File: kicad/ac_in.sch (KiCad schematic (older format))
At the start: 32 parts, among them J701 tblock, U702 R-78E3.3-1.0, U704 R-78E5.0-1.0, U705 AP2114H-1.2TRG1, U706 AP2114H-1.2TRG1

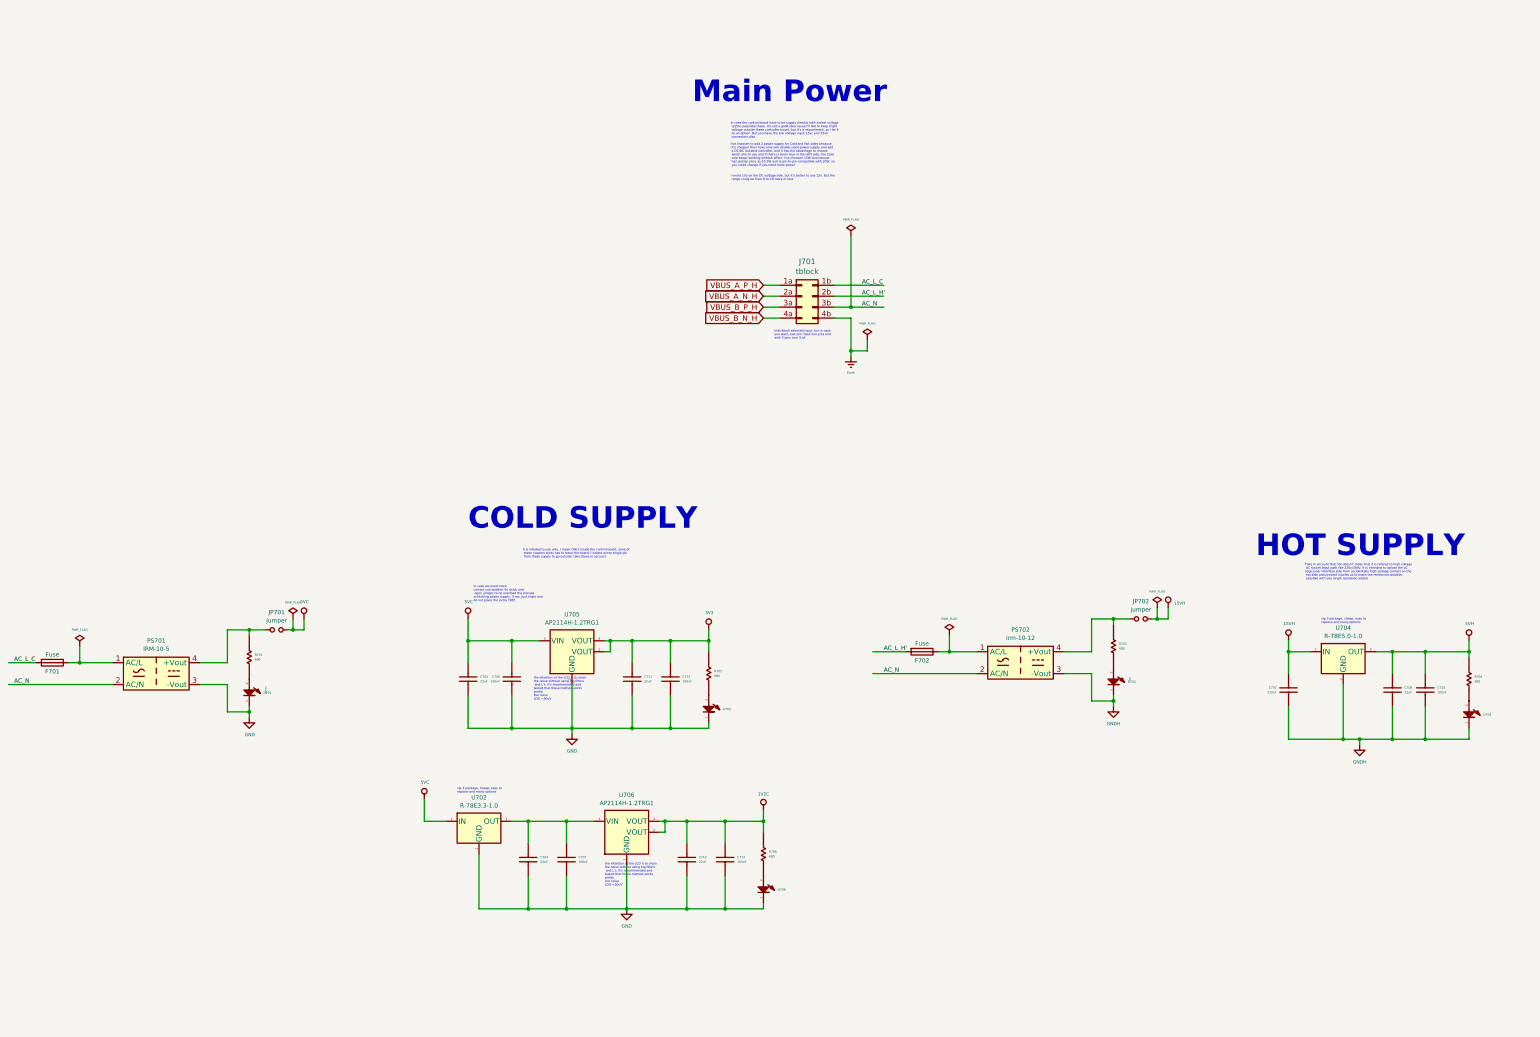
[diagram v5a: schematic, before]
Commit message: mofifing ac/dc position and 3 idc out to 2
I've triung to reacomodate the ac/dc power supplies to manage isolation
and free space using 2 idc instead of 3
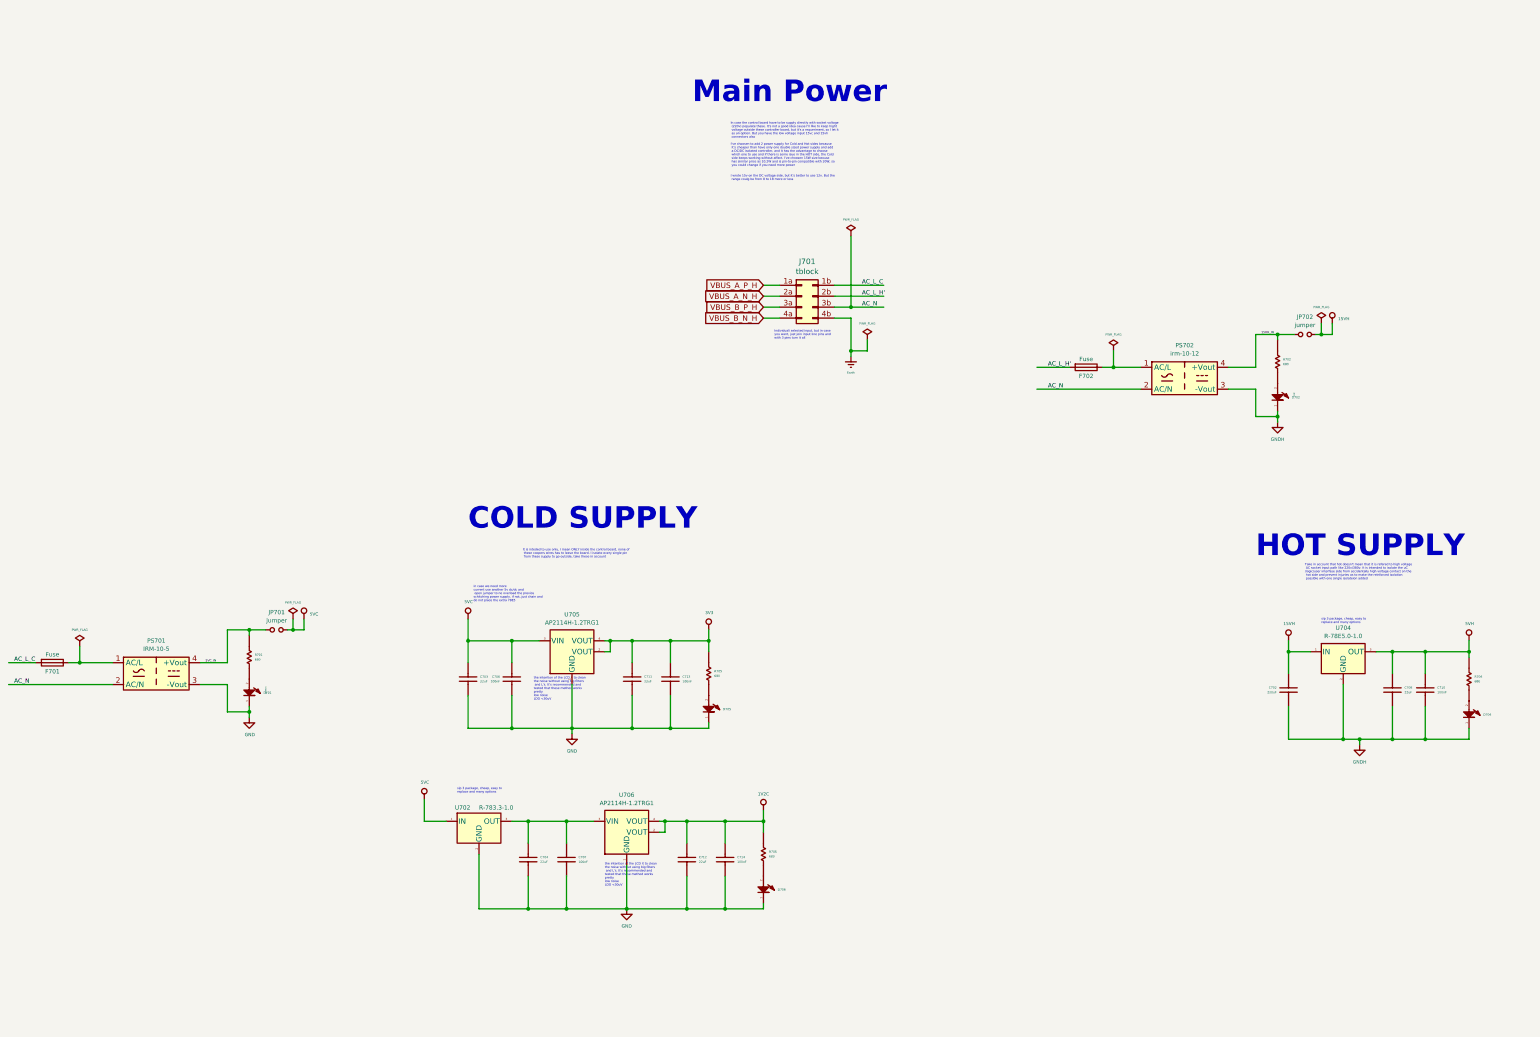
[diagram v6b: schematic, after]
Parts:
- U702: value R-78E3.3-1.0 -> R-783.3-1.0
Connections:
- net labels added: 15VH_IN, 5VC_IN
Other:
- moved on the sheet: D702, F702, JP702, PS702, R702
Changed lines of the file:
@@
 L servo:15VH #PWR0704
 U 1 1 5E18DDCC
-P 11900 6250
-F 0 "#PWR0704" H 11900 6050 20  0001 C CNN
-F 1 "15VH" H 11953 6294 28  0000 L CNN
-F 2 "" H 11900 6250 50  0001 C CNN
-F 3 "" H 11900 6250 50  0001 C CNN
-	1    11900 6250
+P 13400 3650
+F 0 "#PWR0704" H 13400 3450 20  0001 C CNN
+F 1 "15VH" H 13453 3694 28  0000 L CNN
+F 2 "" H 13400 3650 50  0001 C CNN
+F 3 "" H 13400 3650 50  0001 C CNN
+	1    13400 3650
 	1    0    0    -1
 $EndComp
@@
 L servo:GNDH #PWR0702
 U 1 1 5E18DDCD
-P 11400 7150
-F 0 "#PWR0702" H 11400 6900 30  0001 C CNN
-F 1 "GNDH" H 11400 6992 30  0000 C CNN
-F 2 "" H 11400 7150 50  0001 C CNN
-F 3 "" H 11400 7150 50  0001 C CNN
-	1    11400 7150
+P 12900 4550
+F 0 "#PWR0702" H 12900 4300 30  0001 C CNN
+F 1 "GNDH" H 12900 4392 30  0000 C CNN
+F 2 "" H 12900 4550 50  0001 C CNN
+F 3 "" H 12900 4550 50  0001 C CNN
+	1    12900 4550
 	1    0    0    -1
 $EndComp
@@
 U 1 1 5E18DDB9
 P 5600 8200
-F 0 "U702" H 5600 8418 39  0000 C CNN
-F 1 "R-78E3.3-1.0" H 5600 8343 39  0000 C CNN
+F 0 "U702" H 5450 8325 39  0000 C CNN
+F 1 "R-783.3-1.0" H 5600 8325 39  0000 L CNN
 F 2 "Converter_DCDC:Converter_DCDC_RECOM_R-78E-0.5_THT" H 5650 7950 50  0001 L CIN
-F 3 "https://www.recom-power.com/pdf/Innoline/R-78Exx-1.0.pdf" H 5600 8200 50  0001 C CNN
+F 3 "../doc/datasheets/R-78-1.0.pdf" H 5450 8325 50  0001 C CNN
 	1    5600 8200
 	1    0    0    -1
@@
 Wire Wire Line
 	3500 6450 3650 6450
-Connection ~ 9900 6650
-Wire Wire Line
-	9900 6650 9800 6650
-Wire Wire Line
-	9900 6500 9900 6650
+Connection ~ 11400 4050
+Wire Wire Line
+	11400 4050 11300 4050
+Wire Wire Line
+	11400 3900 11400 4050
 $Comp
 L servo:PWR_FLAG #FLG0703
 U 1 1 5E548503
-P 9900 6500
-F 0 "#FLG0703" H 9900 6575 20  0001 C CNN
-F 1 "PWR_FLAG" H 9900 6650 20  0000 C CNN
-F 2 "" H 9900 6500 50  0001 C CNN
-F 3 "~" H 9900 6500 50  0001 C CNN
-	1    9900 6500
+P 11400 3900
+F 0 "#FLG0703" H 11400 3975 20  0001 C CNN
+F 1 "PWR_FLAG" H 11400 4050 20  0000 C CNN
+F 2 "" H 11400 3900 50  0001 C CNN
+F 3 "~" H 11400 3900 50  0001 C CNN
+	1    11400 3900
 	1    0    0    -1
 $EndComp
@@
 L servo:Fuse F702
 U 1 1 5E548509
-P 9650 6650
-F 0 "F702" V 9730 6650 39  0000 C CNN
-F 1 "Fuse" V 9575 6650 39  0000 C CNN
-F 2 "servo:fuse_3912" V 9580 6650 50  0001 C CNN
-F 3 "../doc/datasheets/fuse_3912pdf" V 9730 6650 50  0001 C CNN
-	1    9650 6650
+P 11150 4050
+F 0 "F702" V 11230 4050 39  0000 C CNN
+F 1 "Fuse" V 11075 4050 39  0000 C CNN
+F 2 "servo:fuse_3912" V 11080 4050 50  0001 C CNN
+F 3 "../doc/datasheets/fuse_3912pdf" V 11230 4050 50  0001 C CNN
+	1    11150 4050
 	0    1    1    0
 $EndComp
@@
 L servo:Resistor R?
 U 1 1 5E548518
-P 11400 6600
+P 12900 4000
 AR Path="/5EAA846A/5E548518" Ref="R?"  Part="1"
 AR Path="/5DD76B18/5E548518" Ref="R702"  Part="1"
-F 0 "R702" V 11378 6650 20  0000 L CNN
-F 1 "680" V 11421 6650 20  0000 L CNN
-F 2 "Resistor_SMD:R_0603_1608Metric" H 10900 6500 60  0001 C CNN
-F 3 "" H 11000 6600 60  0001 C CNN
-F 4 "680" V -1000 7000 60  0001 C CNN "ValueDisplayed"
-	1    11400 6600
+F 0 "R702" V 12878 4050 20  0000 L CNN
+F 1 "680" V 12921 4050 20  0000 L CNN
+F 2 "Resistor_SMD:R_0603_1608Metric" H 12400 3900 60  0001 C CNN
+F 3 "" H 12500 4000 60  0001 C CNN
+F 4 "680" V 500 4400 60  0001 C CNN "ValueDisplayed"
+	1    12900 4000
 	0    1    1    0
 $EndComp
@@
 L servo:LED_A2_K1 D?
 U 1 1 5E548520
-P 11400 6900
+P 12900 4300
 AR Path="/5EAA846A/5E548520" Ref="D?"  Part="1"
 AR Path="/5DD76B18/5E548520" Ref="D702"  Part="1"
-F 0 "D702" V 11425 7030 20  0000 L CNN
-F 1 "red" H 11400 7050 16  0000 C CNN
-F 2 "servo:LED_0603_1608Metric" H 11200 6700 60  0001 C CNN
-F 3 "" H 11200 6700 60  0000 C CNN
-F 4 "red" V -1000 6800 60  0001 C CNN "VALUE"
-	1    11400 6900
+F 0 "D702" V 12925 4430 20  0000 L CNN
+F 1 "red" H 12900 4450 16  0000 C CNN
+F 2 "servo:LED_0603_1608Metric" H 12700 4100 60  0001 C CNN
+F 3 "" H 12700 4100 60  0000 C CNN
+F 4 "red" V 500 4200 60  0001 C CNN "VALUE"
+	1    12900 4300
 	0    1    1    0
 $EndComp
 Wire Wire Line
-	11400 7050 11400 7100
-Wire Wire Line
-	11200 7100 11200 6850
-Wire Wire Line
-	11200 6650 11200 6350
-Wire Wire Line
-	11200 6350 11400 6350
-Wire Wire Line
-	11400 6400 11400 6350
-Connection ~ 11400 6350
+	12900 4450 12900 4500
+Wire Wire Line
+	12700 4500 12700 4250
+Wire Wire Line
+	12700 4050 12700 3750
+Wire Wire Line
+	12700 3750 12900 3750
+Wire Wire Line
+	12900 3800 12900 3750
+Connection ~ 12900 3750
 $Comp
 L servo:jumper JP702
 U 1 1 5E54852F
-P 11650 6350
-F 0 "JP702" H 11650 6511 39  0000 C CNN
-F 1 "jumper" H 11650 6436 39  0000 C CNN
-F 2 "servo:SolderJumper-2_P1.3mm_Open_RoundedPad1.0x1.5mm" H 11550 6330 50  0001 C CNN
-F 3 "~" H 11650 6430 50  0001 C CNN
-	1    11650 6350
-	1    0    0    -1
-$EndComp
-Wire Wire Line
-	11750 6350 11800 6350
-Wire Wire Line
-	11900 6250 11900 6350
-Wire Wire Line
-	11400 6350 11550 6350
-Wire Wire Line
-	11400 7150 11400 7100
-Connection ~ 11400 7100
-Wire Wire Line
-	11200 7100 11400 7100
+P 13150 3750
+F 0 "JP702" H 13150 3911 39  0000 C CNN
+F 1 "jumper" H 13150 3836 39  0000 C CNN
+F 2 "servo:SolderJumper-2_P1.3mm_Open_RoundedPad1.0x1.5mm" H 13050 3730 50  0001 C CNN
+F 3 "~" H 13150 3830 50  0001 C CNN
+	1    13150 3750
+	1    0    0    -1
+$EndComp
+Wire Wire Line
+	13250 3750 13300 3750
+Wire Wire Line
+	13400 3650 13400 3750
+Wire Wire Line
+	12900 3750 13050 3750
+Wire Wire Line
+	12900 4550 12900 4500
+Connection ~ 12900 4500
+Wire Wire Line
+	12700 4500 12900 4500
 Wire Wire Line
 	3500 7200 3500 7250
 Connection ~ 3500 7200
 Wire Wire Line
-	11800 6250 11800 6350
+	13300 3650 13300 3750
 $Comp
 L servo:PWR_FLAG #FLG0705
 U 1 1 5E6B6A83
-P 11800 6250
-F 0 "#FLG0705" H 11800 6325 20  0001 C CNN
-F 1 "PWR_FLAG" H 11800 6400 20  0000 C CNN
-F 2 "" H 11800 6250 50  0001 C CNN
-F 3 "~" H 11800 6250 50  0001 C CNN
-	1    11800 6250
-	1    0    0    -1
-$EndComp
-Connection ~ 11800 6350
-Wire Wire Line
-	11800 6350 11900 6350
+P 13300 3650
+F 0 "#FLG0705" H 13300 3725 20  0001 C CNN
+F 1 "PWR_FLAG" H 13300 3800 20  0000 C CNN
+F 2 "" H 13300 3650 50  0001 C CNN
+F 3 "~" H 13300 3650 50  0001 C CNN
+	1    13300 3650
+	1    0    0    -1
+$EndComp
+Connection ~ 13300 3750
+Wire Wire Line
+	13300 3750 13400 3750
 $Comp
 L servo:PWR_FLAG #FLG0704
@@
 	1300 6750 1550 6750
 Wire Wire Line
-	9200 6650 9500 6650
+	10700 4050 11000 4050
 $Comp
 L Connector_Generic:Conn_02x04_Row_Letter_Last J?
@@
 P 4000 6350
 F 0 "#PWR0126" H 4000 6150 20  0001 C CNN
-F 1 "5VC" H 4005 6507 28  0000 C CNN
+F 1 "5VC" H 4053 6394 28  0000 L CNN
 F 2 "" H 4000 6350 50  0001 C CNN
 F 3 "" H 4000 6350 50  0001 C CNN
@@
 L servo:irm-10-12 PS702
 U 1 1 5E299A6A
-P 10550 6750
-F 0 "PS702" H 10550 7051 39  0000 C CNN
-F 1 "irm-10-12" H 10550 6976 39  0000 C CNN
-F 2 "servo:Converter_ACDC_MeanWell_IRM-10-xx_THT" H 10550 6450 50  0001 C CNN
-F 3 "../doc/datasheets/irm-10.pdf" H 10950 6400 50  0001 C CNN
-	1    10550 6750
-	1    0    0    -1
-$EndComp
-Wire Wire Line
-	9900 6650 10150 6650
-Wire Wire Line
-	10950 6650 11200 6650
-Wire Wire Line
-	10950 6850 11200 6850
+P 12050 4150
+F 0 "PS702" H 12050 4451 39  0000 C CNN
+F 1 "irm-10-12" H 12050 4376 39  0000 C CNN
+F 2 "servo:Converter_ACDC_MeanWell_IRM-10-xx_THT" H 12050 3850 50  0001 C CNN
+F 3 "../doc/datasheets/irm-10.pdf" H 12450 3800 50  0001 C CNN
+	1    12050 4150
+	1    0    0    -1
+$EndComp
+Wire Wire Line
+	11400 4050 11650 4050
+Wire Wire Line
+	12450 4050 12700 4050
+Wire Wire Line
+	12450 4250 12700 4250
 Wire Wire Line
 	5100 8000 5100 8200
@@
 	9000 3900 9000 3950
 Wire Wire Line
-	9200 6850 10150 6850
+	10700 4250 11650 4250
 Wire Wire Line
 	9000 2850 9000 3500
@@
 Text Label 1350 6750 0    39   ~ 0
 AC_L_C
-Text Label 9300 6650 0    39   ~ 0
+Text Label 10800 4050 0    39   ~ 0
 AC_L_H'
-Text Label 9300 6850 0    39   ~ 0
+Text Label 10800 4250 0    39   ~ 0
 AC_N
 Text Label 1350 6950 0    39   ~ 0
 AC_N
+Text Label 12750 3750 0    20   ~ 0
+15VH_IN
+Text Label 3100 6750 0    20   ~ 0
+5VC_IN
 $EndSCHEMATC

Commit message: beginine routing... far far away
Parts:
- removed C703, C711: 22uF, servo:C_0603_1608Metric, symbol servo:Capacitor
- removed C706, C707, C713: 100nF, servo:C_0603_1608Metric, symbol servo:Capacitor
- removed U705: AP2114H-1.2TRG1, Package_TO_SOT_SMD:SOT-223, symbol servo:AP2114
- added C701: 22uF, servo:C_0603_1608Metric, symbol servo:Capacitor
- U702: value R-783.3-1.0 -> R-78B3.3-2.0
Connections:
- net labels added: AC_L_C_FUSE, AC_L_H, AC_L_H_FUSE, VBUS1_N_H, VBUS1_P_H, VBUS2_N_H, VBUS2_P_H
- net labels removed: AC_L_H', VBUS_A_N_H, VBUS_A_P_H, VBUS_B_N_H, VBUS_B_P_H
- wire segments 130 -> 108
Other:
- note removed: "in case we need more \ncurrent use another 5v dc/dc and\n open jumper to no overload the previos \nschitching power supply. if not, just chain and \ndo not place the extra 78E5"
- moved on the sheet: C702, C704, C708, C710, C712, C714, D701, D702, D704, D705, D706, F701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
